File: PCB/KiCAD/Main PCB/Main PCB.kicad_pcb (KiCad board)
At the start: 2 copper layers, 120 x 120 mm, 0 parts

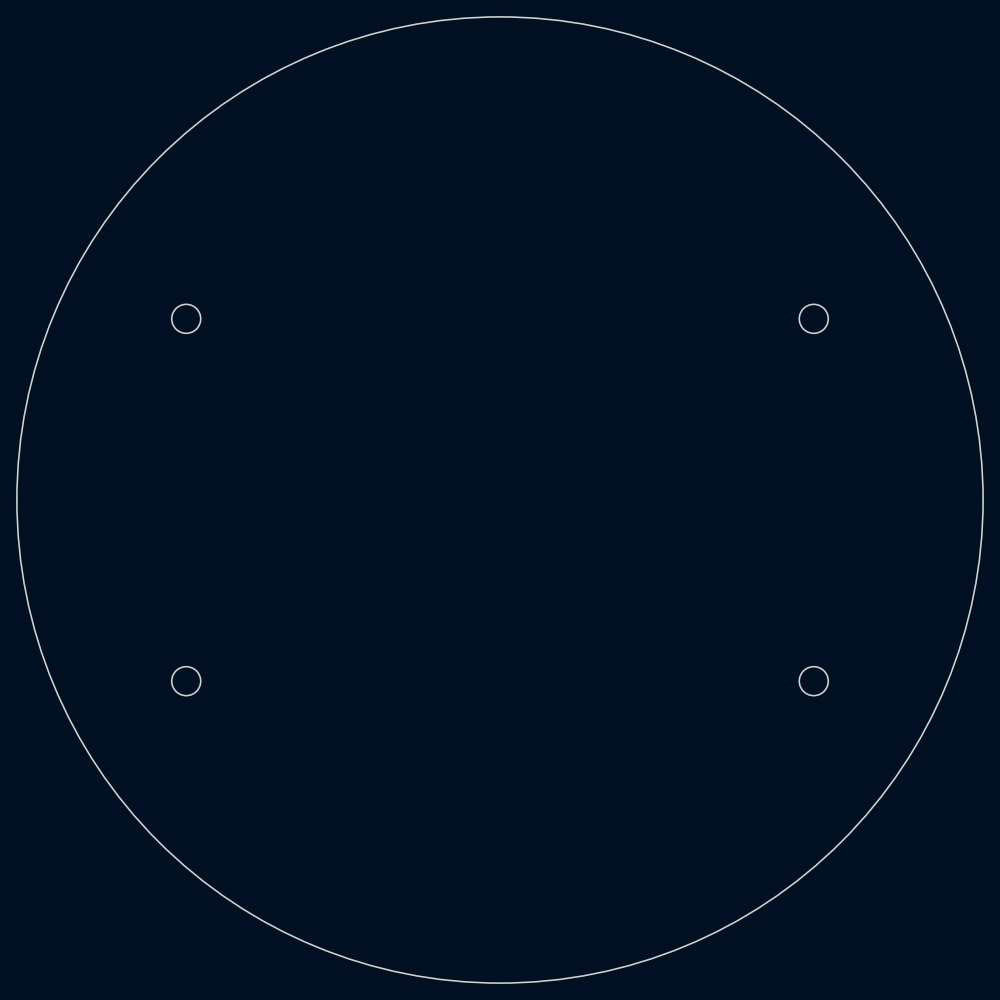
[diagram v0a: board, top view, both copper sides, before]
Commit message: Start to upper PCB
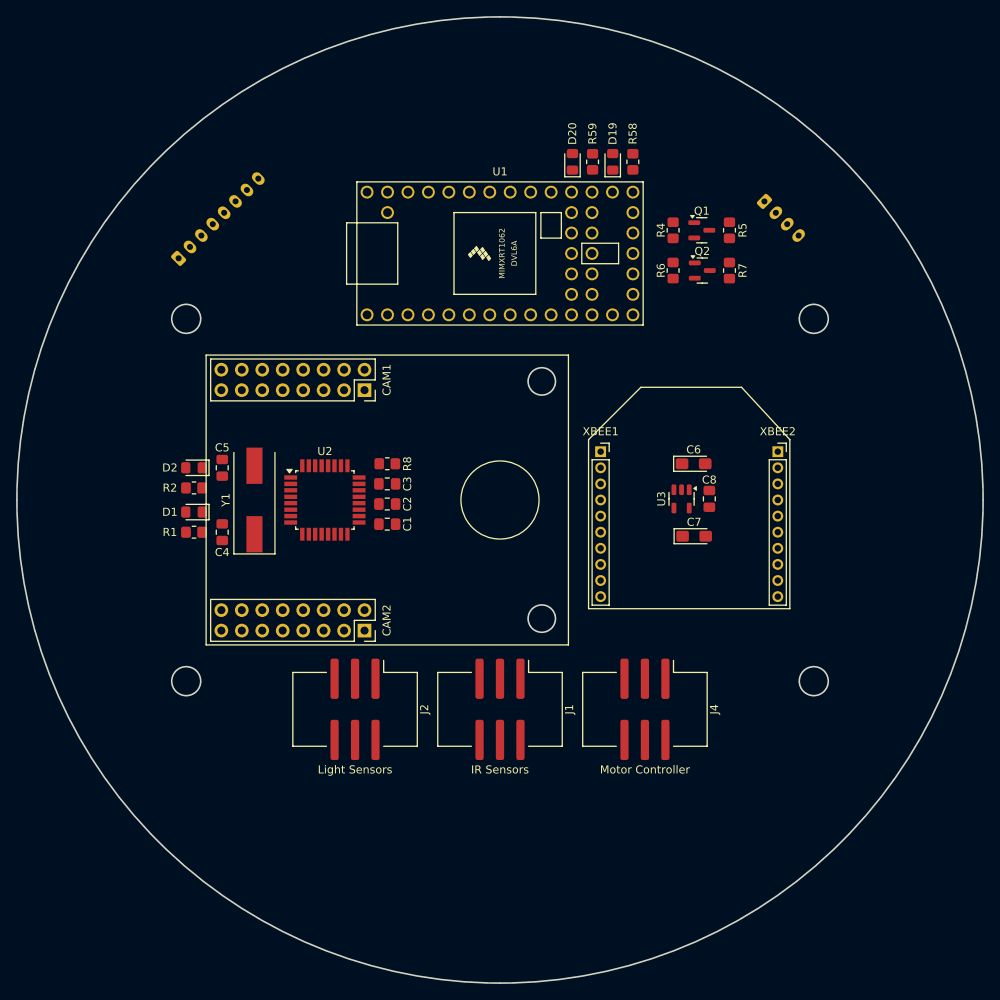
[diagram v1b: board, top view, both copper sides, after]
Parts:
- added C1: 100nF, Capacitor_SMD:C_0805_2012Metric_Pad1.18x1.45mm_HandSolder, F.Cu at (-14.0, 3.00)
- added C2: 100nF, Capacitor_SMD:C_0805_2012Metric_Pad1.18x1.45mm_HandSolder, F.Cu at (-14.0, 0.50)
- added C3: 100nF, Capacitor_SMD:C_0805_2012Metric_Pad1.18x1.45mm_HandSolder, F.Cu at (-14.0, -2.00)
- added C4: 22pF, Capacitor_SMD:C_0805_2012Metric_Pad1.18x1.45mm_HandSolder, F.Cu at (-34.5, 4.00)
- added C5: 22pF, Capacitor_SMD:C_0805_2012Metric_Pad1.18x1.45mm_HandSolder, F.Cu at (-34.5, -4.00)
- added C6: 10uF, Capacitor_Tantalum_SMD:CP_EIA-3216-12_Kemet-S_Pad1.58x1.35mm_HandSolder, F.Cu at (24.1, -4.50)
- added C7: 10uF, Capacitor_Tantalum_SMD:CP_EIA-3216-12_Kemet-S_Pad1.58x1.35mm_HandSolder, F.Cu at (24.1, 4.50)
- added C8: 0.1uF, Capacitor_SMD:C_0805_2012Metric_Pad1.18x1.45mm_HandSolder, F.Cu at (26.0, -0.14)
- added CAM1: Conn_02x08_Top_Bottom, Connector_PinSocket_2.54mm:PinSocket_2x08_P2.54mm_Vertical, F.Cu at (-16.8, -13.6)
- added CAM2: Conn_02x08_Top_Bottom, Connector_PinSocket_2.54mm:PinSocket_2x08_P2.54mm_Vertical, F.Cu at (-16.8, 16.2)
- added D1: GREEN_LED, LED_SMD:LED_0805_2012Metric_Pad1.15x1.40mm_HandSolder, F.Cu at (-38.0, 1.50)
- added D19: RED_LED, LED_SMD:LED_0805_2012Metric_Pad1.15x1.40mm_HandSolder, F.Cu at (14.0, -42.0)
- added D2: RED_LED, LED_SMD:LED_0805_2012Metric_Pad1.15x1.40mm_HandSolder, F.Cu at (-38.0, -4.00)
- added D20: GREEN_LED, LED_SMD:LED_0805_2012Metric_Pad1.15x1.40mm_HandSolder, F.Cu at (9.00, -42.0)
- added J1: Conn_02x03_Odd_Even, Connector_IDC:IDC-Header_2x03_P2.54mm_Vertical_SMD, F.Cu at (0.00, 26.0)
- added J2: Conn_02x03_Odd_Even, Connector_IDC:IDC-Header_2x03_P2.54mm_Vertical_SMD, F.Cu at (-18.0, 26.0)
- added J3: Conn_01x04, Connector_JST:JST_PH_B4B-PH-K_1x04_P2.00mm_Vertical, B.Cu at (32.8, -37.1)
- added J4: Conn_02x03_Odd_Even, Connector_IDC:IDC-Header_2x03_P2.54mm_Vertical_SMD, F.Cu at (18.0, 26.0)
- added J5: Conn_01x08, Connector_JST:JST_PH_B8B-PH-K_1x08_P2.00mm_Vertical, B.Cu at (-39.9, -30.0)
- added Q1: BSS138, Package_TO_SOT_SMD:SOT-23, F.Cu at (25.1, -33.5)
- added Q2: BSS138, Package_TO_SOT_SMD:SOT-23, F.Cu at (25.1, -28.5)
- added R1: 330, Resistor_SMD:R_0805_2012Metric_Pad1.20x1.40mm_HandSolder, F.Cu at (-38.0, 4.00)
- added R2: 330, Resistor_SMD:R_0805_2012Metric_Pad1.20x1.40mm_HandSolder, F.Cu at (-38.0, -1.50)
- added R4: 10k, Resistor_SMD:R_0805_2012Metric_Pad1.20x1.40mm_HandSolder, F.Cu at (21.5, -33.5)
- added R5: 10k, Resistor_SMD:R_0805_2012Metric_Pad1.20x1.40mm_HandSolder, F.Cu at (28.5, -33.5)
- added R58: 330, Resistor_SMD:R_0805_2012Metric_Pad1.20x1.40mm_HandSolder, F.Cu at (16.5, -42.0)
- added R59: 330, Resistor_SMD:R_0805_2012Metric_Pad1.20x1.40mm_HandSolder, F.Cu at (11.5, -42.0)
- added R6: 10k, Resistor_SMD:R_0805_2012Metric_Pad1.20x1.40mm_HandSolder, F.Cu at (21.5, -28.5)
- added R7: 10k, Resistor_SMD:R_0805_2012Metric_Pad1.20x1.40mm_HandSolder, F.Cu at (28.5, -28.5)
- added R8: 10k, Resistor_SMD:R_0805_2012Metric_Pad1.20x1.40mm_HandSolder, F.Cu at (-14.0, -4.50)
- added U1: Teensy4.0, Teensy:Teensy40, F.Cu at (0.00, -30.6)
- added U2: ATmega328PB-A, Package_QFP:TQFP-32_7x7mm_P0.8mm, F.Cu at (-21.8, 0.00)
- added U3: MIC5219-3.3YM5, Package_TO_SOT_SMD:SOT-23-5, F.Cu at (22.6, -0.14)
- added XBEE1: Conn_01x10, Connector_PinSocket_2.00mm:PinSocket_1x10_P2.00mm_Vertical, F.Cu at (12.5, -6.00)
- added XBEE2: Conn_01x10, Connector_PinSocket_2.00mm:PinSocket_1x10_P2.00mm_Vertical, F.Cu at (34.5, -6.00)
- added Y1: Crystal, Crystal:Crystal_SMD_HC49-SD, F.Cu at (-30.5, 0.00)
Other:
- outline, holes or cut-outs redrawn
- board text added: "IR Sensors"
- board text added: "Light Sensors"
- board text added: "MISO"
- board text added: "MOSI"
- board text added: "Motor Controller"
- board text added: "RESET"
- board text added: "SCK"
- board text added: "U1"
- board text added: "U6"

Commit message: More work to main PCB
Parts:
- added C32: 100nF, Capacitor_SMD:C_0805_2012Metric_Pad1.18x1.45mm_HandSolder, F.Cu at (-13.0, 7.50)
- added C33: 100nF, Capacitor_SMD:C_0805_2012Metric_Pad1.18x1.45mm_HandSolder, F.Cu at (-13.0, -7.00)
- added C9: C_Polarized, Capacitor_SMD:CP_Elec_4x5.4, F.Cu at (0.50, 49.5)
- added IC1: TSSP4038, TSOP4038:TSSP4038, F.Cu at (0.54, 56.0)
- added IC2: ADG608BRZ, ADG608BRZ:SOIC127P600X175-16N, F.Cu at (-6.00, 7.50)
- added IC3: ADG608BRZ, ADG608BRZ:SOIC127P600X175-16N, F.Cu at (-6.00, -7.00)
- added R19: 100, Resistor_SMD:R_0805_2012Metric_Pad1.20x1.40mm_HandSolder, F.Cu at (5.50, 53.0)
- moved C1 1.00 mm to (-14.0, 4.00)
- moved C2 1.00 mm to (-14.0, 1.50)
- moved C3 1.00 mm to (-14.0, -1.00)
- moved R8 1.00 mm to (-14.0, -3.50)
- moved U3 0.57 mm to (22.0, 0.00)
- moved C8 0.14 mm to (26.0, 0.00)
- moved C7 0.11 mm to (24.0, 4.50)
- moved C6 0.05 mm to (24.0, -4.50)

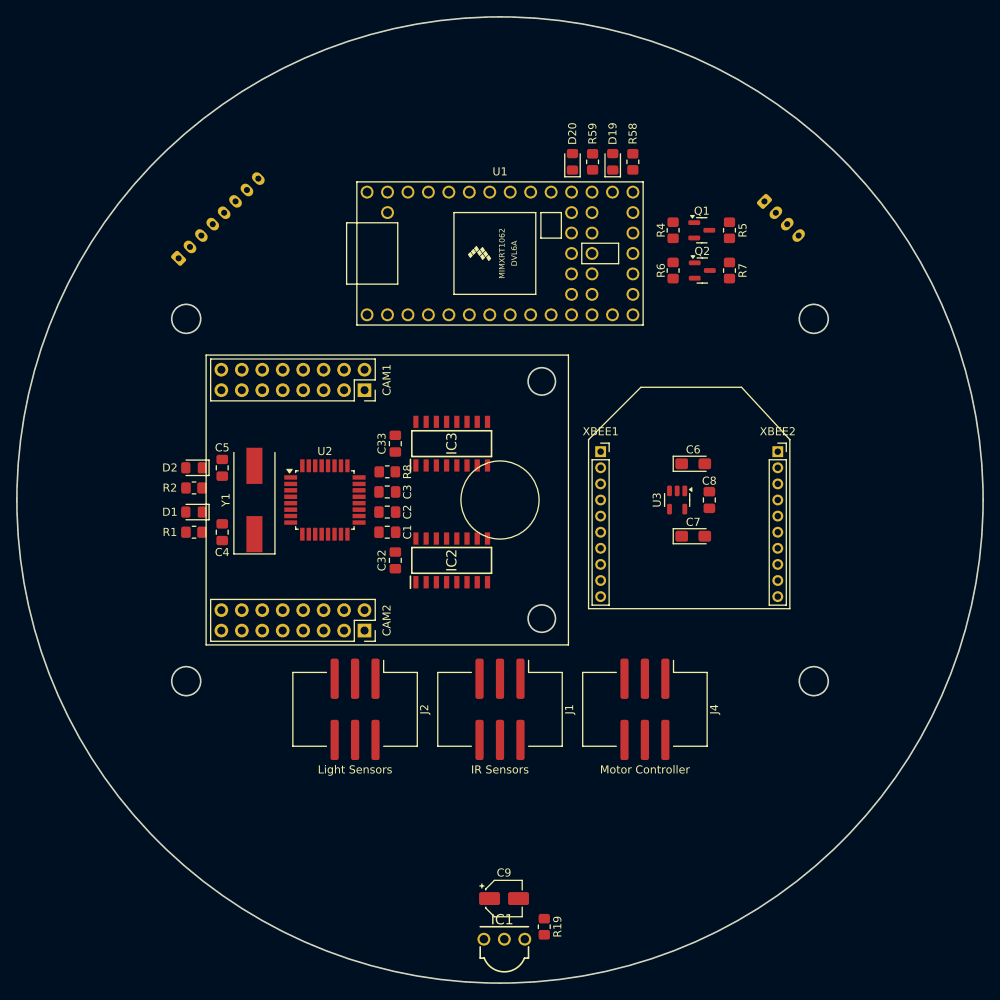
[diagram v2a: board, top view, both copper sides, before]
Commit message: More work to the Main PCB and refinement of Via sizes
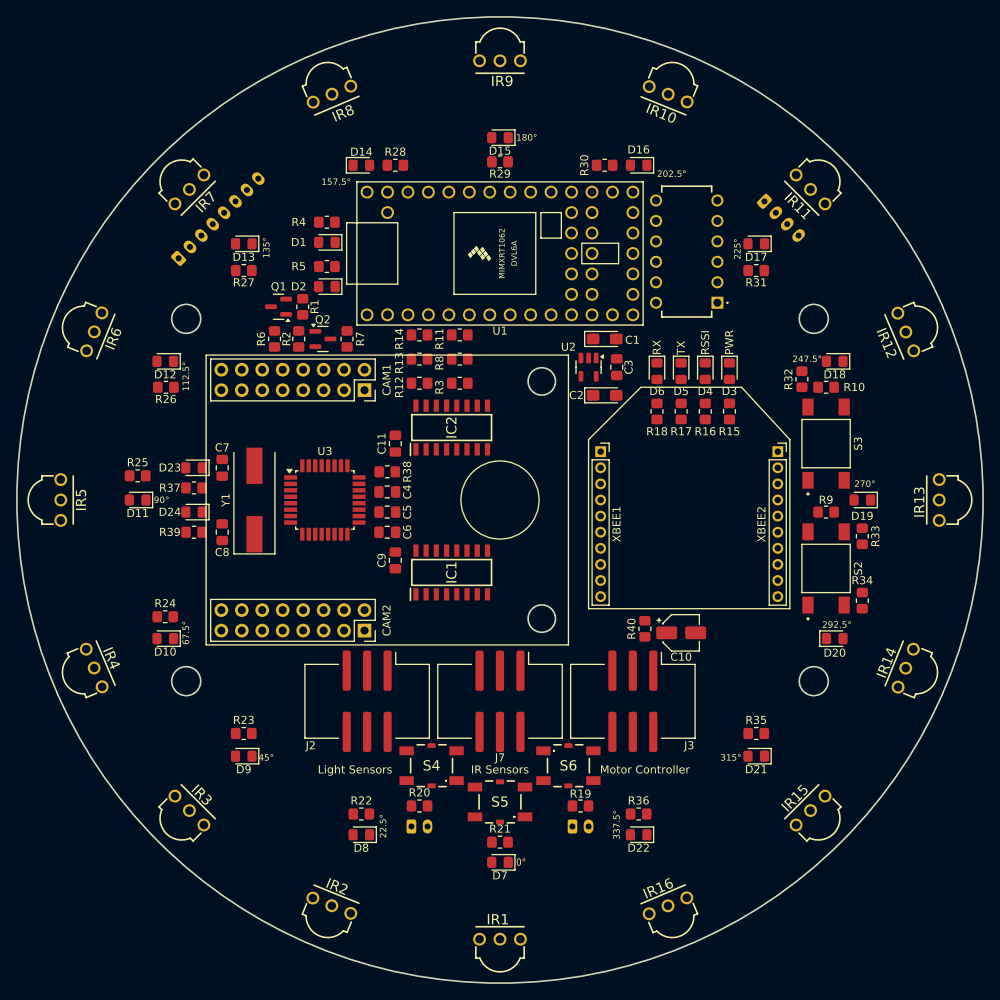
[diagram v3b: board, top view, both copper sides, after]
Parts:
- added D10: BALL_DIR_LED, LED_SMD:LED_0805_2012Metric_Pad1.15x1.40mm_HandSolder, F.Cu at (-41.6, 17.2)
- added D11: BALL_DIR_LED, LED_SMD:LED_0805_2012Metric_Pad1.15x1.40mm_HandSolder, F.Cu at (-45.0, 0.00)
- added D12: BALL_DIR_LED, LED_SMD:LED_0805_2012Metric_Pad1.15x1.40mm_HandSolder, F.Cu at (-41.6, -17.2)
- added D13: BALL_DIR_LED, LED_SMD:LED_0805_2012Metric_Pad1.15x1.40mm_HandSolder, F.Cu at (-31.8, -31.8)
- added D14: BALL_DIR_LED, LED_SMD:LED_0805_2012Metric_Pad1.15x1.40mm_HandSolder, F.Cu at (-17.2, -41.6)
- added D15: BALL_DIR_LED, LED_SMD:LED_0805_2012Metric_Pad1.15x1.40mm_HandSolder, F.Cu at (0.00, -45.0)
- added D16: BALL_DIR_LED, LED_SMD:LED_0805_2012Metric_Pad1.15x1.40mm_HandSolder, F.Cu at (17.2, -41.6)
- added D17: BALL_DIR_LED, LED_SMD:LED_0805_2012Metric_Pad1.15x1.40mm_HandSolder, F.Cu at (31.8, -31.8)
- added D18: BALL_DIR_LED, LED_SMD:LED_0805_2012Metric_Pad1.15x1.40mm_HandSolder, F.Cu at (41.6, -17.2)
- added D19: BALL_DIR_LED, LED_SMD:LED_0805_2012Metric_Pad1.15x1.40mm_HandSolder, F.Cu at (45.0, 0.00)
- added D20: BALL_DIR_LED, LED_SMD:LED_0805_2012Metric_Pad1.15x1.40mm_HandSolder, F.Cu at (41.6, 17.2)
- added D21: BALL_DIR_LED, LED_SMD:LED_0805_2012Metric_Pad1.15x1.40mm_HandSolder, F.Cu at (31.8, 31.8)
- added D22: BALL_DIR_LED, LED_SMD:LED_0805_2012Metric_Pad1.15x1.40mm_HandSolder, F.Cu at (17.2, 41.6)
- added D3: LED, LED_SMD:LED_0805_2012Metric_Pad1.15x1.40mm_HandSolder, F.Cu at (28.5, -16.0)
- added D4: LED, LED_SMD:LED_0805_2012Metric_Pad1.15x1.40mm_HandSolder, F.Cu at (25.5, -16.0)
- added D5: LED, LED_SMD:LED_0805_2012Metric_Pad1.15x1.40mm_HandSolder, F.Cu at (22.5, -16.0)
- added D6: LED, LED_SMD:LED_0805_2012Metric_Pad1.15x1.40mm_HandSolder, F.Cu at (19.5, -16.0)
- added D7: BALL_DIR_LED, LED_SMD:LED_0805_2012Metric_Pad1.15x1.40mm_HandSolder, F.Cu at (0.00, 45.0)
- added D8: BALL_DIR_LED, LED_SMD:LED_0805_2012Metric_Pad1.15x1.40mm_HandSolder, F.Cu at (-17.2, 41.6)
- added D9: BALL_DIR_LED, LED_SMD:LED_0805_2012Metric_Pad1.15x1.40mm_HandSolder, F.Cu at (-31.8, 31.8)
- added IR10: TSSP4038, TSOP4038:TSSP4038, F.Cu at (21.4, -51.7)
- added IR11: TSSP4038, TSOP4038:TSSP4038, F.Cu at (39.6, -39.6)
- added IR12: TSSP4038, TSOP4038:TSSP4038, F.Cu at (51.7, -21.4)
- added IR13: TSSP4038, TSOP4038:TSSP4038, F.Cu at (56.0, 0.00)
- added IR14: TSSP4038, TSOP4038:TSSP4038, F.Cu at (51.7, 21.4)
- added IR15: TSSP4038, TSOP4038:TSSP4038, F.Cu at (39.6, 39.6)
- added IR16: TSSP4038, TSOP4038:TSSP4038, F.Cu at (21.4, 51.7)
- added IR2: TSSP4038, TSOP4038:TSSP4038, F.Cu at (-21.4, 51.7)
- added IR3: TSSP4038, TSOP4038:TSSP4038, F.Cu at (-39.6, 39.6)
- added IR4: TSSP4038, TSOP4038:TSSP4038, F.Cu at (-51.7, 21.4)
- added IR5: TSSP4038, TSOP4038:TSSP4038, F.Cu at (-56.0, 0.00)
- added IR6: TSSP4038, TSOP4038:TSSP4038, F.Cu at (-51.7, -21.4)
- added IR7: TSSP4038, TSOP4038:TSSP4038, F.Cu at (-39.6, -39.6)
- added IR8: TSSP4038, TSOP4038:TSSP4038, F.Cu at (-21.4, -51.7)
- added IR9: TSSP4038, TSOP4038:TSSP4038, F.Cu at (0.00, -56.0)
- added J5: Conn_01x02, Connector_JST:JST_PH_B2B-PH-K_1x02_P2.00mm_Vertical, B.Cu at (-11.0, 40.5)
- added J6: Conn_01x02, Connector_JST:JST_PH_B2B-PH-K_1x02_P2.00mm_Vertical, B.Cu at (9.00, 40.5)
- added R10: 4.7k, Resistor_SMD:R_0805_2012Metric_Pad1.20x1.40mm_HandSolder, F.Cu at (40.5, -14.0)
- added R11: 4.7k, Resistor_SMD:R_0805_2012Metric_Pad1.20x1.40mm_HandSolder, F.Cu at (-5.00, -20.5)
- added R12: 4.7k, Resistor_SMD:R_0805_2012Metric_Pad1.20x1.40mm_HandSolder, F.Cu at (-10.0, -14.5)
- added R13: 4.7k, Resistor_SMD:R_0805_2012Metric_Pad1.20x1.40mm_HandSolder, F.Cu at (-10.0, -17.5)
- added R14: 4.7k, Resistor_SMD:R_0805_2012Metric_Pad1.20x1.40mm_HandSolder, F.Cu at (-10.0, -20.5)
- added R15: 1k, Resistor_SMD:R_0805_2012Metric_Pad1.20x1.40mm_HandSolder, F.Cu at (28.5, -11.0)
- added R16: 1k, Resistor_SMD:R_0805_2012Metric_Pad1.20x1.40mm_HandSolder, F.Cu at (25.5, -11.0)
- added R17: 1k, Resistor_SMD:R_0805_2012Metric_Pad1.20x1.40mm_HandSolder, F.Cu at (22.5, -11.0)
- added R18: 1k, Resistor_SMD:R_0805_2012Metric_Pad1.20x1.40mm_HandSolder, F.Cu at (19.5, -11.0)
- added R19: 10k, Resistor_SMD:R_0805_2012Metric_Pad1.20x1.40mm_HandSolder, F.Cu at (10.0, 38.0)
- added R20: 82, Resistor_SMD:R_0805_2012Metric_Pad1.20x1.40mm_HandSolder, F.Cu at (-10.0, 38.0)
- added R21: 130, Resistor_SMD:R_0805_2012Metric_Pad1.20x1.40mm_HandSolder, F.Cu at (0.00, 42.5)
- added R22: 130, Resistor_SMD:R_0805_2012Metric_Pad1.20x1.40mm_HandSolder, F.Cu at (-17.2, 39.0)
- added R23: 130, Resistor_SMD:R_0805_2012Metric_Pad1.20x1.40mm_HandSolder, F.Cu at (-31.8, 29.0)
- added R24: 130, Resistor_SMD:R_0805_2012Metric_Pad1.20x1.40mm_HandSolder, F.Cu at (-41.6, 14.5)
- added R25: 130, Resistor_SMD:R_0805_2012Metric_Pad1.20x1.40mm_HandSolder, F.Cu at (-45.0, -3.00)
- added R26: 130, Resistor_SMD:R_0805_2012Metric_Pad1.20x1.40mm_HandSolder, F.Cu at (-41.5, -14.0)
- added R27: 130, Resistor_SMD:R_0805_2012Metric_Pad1.20x1.40mm_HandSolder, F.Cu at (-31.8, -28.5)
- added R28: 130, Resistor_SMD:R_0805_2012Metric_Pad1.20x1.40mm_HandSolder, F.Cu at (-13.0, -41.6)
- added R29: 130, Resistor_SMD:R_0805_2012Metric_Pad1.20x1.40mm_HandSolder, F.Cu at (0.00, -42.0)
- added R3: 4.7k, Resistor_SMD:R_0805_2012Metric_Pad1.20x1.40mm_HandSolder, F.Cu at (-5.00, -14.5)
- added R30: 130, Resistor_SMD:R_0805_2012Metric_Pad1.20x1.40mm_HandSolder, F.Cu at (13.0, -41.6)
- added R31: 130, Resistor_SMD:R_0805_2012Metric_Pad1.20x1.40mm_HandSolder, F.Cu at (31.8, -28.5)
- added R32: 130, Resistor_SMD:R_0805_2012Metric_Pad1.20x1.40mm_HandSolder, F.Cu at (37.5, -15.0)
- added R33: 130, Resistor_SMD:R_0805_2012Metric_Pad1.20x1.40mm_HandSolder, F.Cu at (45.0, 4.50)
- added R34: 130, Resistor_SMD:R_0805_2012Metric_Pad1.20x1.40mm_HandSolder, F.Cu at (45.0, 12.5)
- added R35: 130, Resistor_SMD:R_0805_2012Metric_Pad1.20x1.40mm_HandSolder, F.Cu at (31.8, 29.0)
- added R36: 130, Resistor_SMD:R_0805_2012Metric_Pad1.20x1.40mm_HandSolder, F.Cu at (17.2, 39.0)
- added R8: 4.7k, Resistor_SMD:R_0805_2012Metric_Pad1.20x1.40mm_HandSolder, F.Cu at (-5.00, -17.5)
- added R9: 4.7k, Resistor_SMD:R_0805_2012Metric_Pad1.20x1.40mm_HandSolder, F.Cu at (40.5, 1.50)
- added S1: 2454982-4, DIP_SW_6:DIP_6_SWITCH_THT, F.Cu at (27.0, -24.5)
- added S2: TS04-SMT, TS04:SW_TS04-66-70-BK-260-SMT, F.Cu at (40.5, 8.50)
- added S3: TS04-SMT, TS04:SW_TS04-66-70-BK-260-SMT, F.Cu at (40.5, -7.00)
- added S4: MSLPT5252BG4MTR, MSLPT5252BG4MTR:MSLPT5252BG4MTR, F.Cu at (-8.50, 33.0)
- added S5: MSLPT5252BG4MTR, MSLPT5252BG4MTR:MSLPT5252BG4MTR, F.Cu at (0.00, 37.5)
- added S6: MSLPT5252BG4MTR, MSLPT5252BG4MTR:MSLPT5252BG4MTR, F.Cu at (8.50, 33.0)
- C10: renamed from C9; value C_Polarized -> 4.7uF
- moved R6 58.1 mm to (-28.0, -20.0), turned to 90 degrees
- moved Q1 53.4 mm to (-27.5, -24.0), turned to 180 degrees
- moved R7 48.3 mm to (-19.0, -20.0)
- moved Q2 47.9 mm to (-22.0, -20.0)
- moved R2 47.3 mm to (-25.0, -20.0)
- moved R1 47.0 mm to (-24.5, -24.0)
- moved C10 39.7 mm to (22.5, 16.5)
- moved R40 39.1 mm to (18.0, 16.0), turned to 90 degrees
- moved R4 38.7 mm to (-21.5, -34.5), turned to 180 degrees
- moved D1 36.9 mm to (-21.5, -32.0), turned to 180 degrees
- moved R5 35.5 mm to (-21.5, -29.0), turned to 180 degrees
- moved D2 34.2 mm to (-21.5, -26.5), turned to 180 degrees
- moved C2 20.7 mm to (13.0, -13.0)
- moved C3 20.1 mm to (14.5, -16.5)
- moved U2 19.8 mm to (11.0, -16.5)
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- renumbered C6 to C1, C33 to C11, C7 to C2, C8 to C3, C3 to C4, C2 to C5, C1 to C6, C5 to C7, C4 to C8, C32 to C9, D19 to D1, D20 to D2, D2 to D23, D1 to D24, IC2 to IC1, IC3 to IC2, IC1 to IR1, J3 to J1, J4 to J3, J5 to J4, J1 to J7, R4 to R1, R6 to R2, R2 to R37, R8 to R38, R1 to R39, R58 to R4, R19 to R40, R59 to R5, R5 to R6, U3 to U2, U2 to U3
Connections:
- net Net-(IC1-VS) renamed TSSP_PWR
- net Net-(J1-Pin_5) renamed RESET_U2
- IC1 pad 10: unconnected-(IC2-S7-Pad10) -> Net-(IC1-S7)
- IC1 pad 11: unconnected-(IC2-S6-Pad11) -> Net-(IC1-S6)
- IC1 pad 12: unconnected-(IC2-S5-Pad12) -> Net-(IC1-S5)
- IC1 pad 5: unconnected-(IC2-S2-Pad5) -> Net-(IC1-S2)
- IC1 pad 6: unconnected-(IC2-S3-Pad6) -> Net-(IC1-S3)
- IC1 pad 7: unconnected-(IC2-S4-Pad7) -> Net-(IC1-S4)
- IC1 pad 9: unconnected-(IC2-S8-Pad9) -> Net-(IC1-S8)
- IC2 pad 10: unconnected-(IC3-S7-Pad10) -> Net-(IC2-S7)
- IC2 pad 11: unconnected-(IC3-S6-Pad11) -> Net-(IC2-S6)
- IC2 pad 12: unconnected-(IC3-S5-Pad12) -> Net-(IC2-S5)
- IC2 pad 4: unconnected-(IC3-S1-Pad4) -> Net-(IC2-S1)
- IC2 pad 5: unconnected-(IC3-S2-Pad5) -> Net-(IC2-S2)
- IC2 pad 6: unconnected-(IC3-S3-Pad6) -> Net-(IC2-S3)
- IC2 pad 7: unconnected-(IC3-S4-Pad7) -> Net-(IC2-S4)
- IC2 pad 9: unconnected-(IC3-S8-Pad9) -> Net-(IC2-S8)
- U1 pad 10: unconnected-(U1-8_TX2_IN1-Pad10) -> CAMERA_TX
- U1 pad 12: unconnected-(U1-10_CS_MQSR-Pad12) -> START_BUTTON
- U1 pad 13: unconnected-(U1-11_MOSI_CTX1-Pad13) -> CALIBRATE_BUTTON
- U1 pad 14: unconnected-(U1-12_MISO_MQSL-Pad14) -> IR_DIR_0
- U1 pad 2: unconnected-(U1-0_RX1_CRX2_CS1-Pad2) -> COM_RX
- U1 pad 21: unconnected-(U1-14_A0_TX3_SPDIF_OUT-Pad21) -> LG_RECEIVE
- U1 pad 22: unconnected-(U1-15_A1_RX3_SPDIF_IN-Pad22) -> IR_DIR_90
- U1 pad 23: unconnected-(U1-16_A2_RX4_SCL1-Pad23) -> IR_DIR_180
- U1 pad 24: unconnected-(U1-17_A3_TX4_SDA1-Pad24) -> IR_DIR_270
- U1 pad 27: unconnected-(U1-20_A6_TX5_LRCLK1-Pad27) -> IR_DIR_45
- U1 pad 28: unconnected-(U1-21_A7_RX5_BCLK1-Pad28) -> IR_DIR_135
- U1 pad 29: unconnected-(U1-22_A8_CTX1-Pad29) -> IR_DIR_225
- U1 pad 3: unconnected-(U1-1_TX1_CTX2_MISO1-Pad3) -> COM_TX
- U1 pad 30: unconnected-(U1-23_A9_CRX1_MCLK1-Pad30) -> IR_DIR_315
- U1 pad 35: unconnected-(U1-24_A10_TX6_SCL2-Pad35) -> IR_DIR_22.5
- U1 pad 36: unconnected-(U1-25_A11_RX6_SDA2-Pad36) -> IR_DIR_67.5
- U1 pad 37: unconnected-(U1-26_A12_MOSI1-Pad37) -> IR_DIR_112.5
- U1 pad 38: unconnected-(U1-27_A13_SCK1-Pad38) -> IR_DIR_157.5
- U1 pad 39: unconnected-(U1-28_RX7-Pad39) -> IR_DIR_202.5
- U1 pad 4: unconnected-(U1-2_OUT2-Pad4) -> Net-(U1-2_OUT2)
- U1 pad 40: unconnected-(U1-29_TX7-Pad40) -> IR_DIR_247.5
- U1 pad 41: unconnected-(U1-30_CRX3-Pad41) -> IR_DIR_292.5
- U1 pad 42: unconnected-(U1-31_CTX3-Pad42) -> IR_DIR_337.5
- U1 pad 43: unconnected-(U1-32_OUT1B-Pad43) -> Net-(U1-32_OUT1B)
- U1 pad 5: unconnected-(U1-3_LRCLK2-Pad5) -> Net-(U1-3_LRCLK2)
- U1 pad 6: unconnected-(U1-4_BCLK2-Pad6) -> Net-(U1-4_BCLK2)
- U1 pad 7: unconnected-(U1-5_IN2-Pad7) -> Net-(U1-5_IN2)
- U1 pad 8: unconnected-(U1-6_OUT1D-Pad8) -> Net-(U1-6_OUT1D)
- U1 pad 9: unconnected-(U1-7_RX2_OUT1A-Pad9) -> CAMERA_RX
- XBEE1 pad 1: +3V3 -> +3V3_XBEE
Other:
- board text added: "0°"
- board text added: "112.5°"
- board text added: "135°"
- board text added: "157.5°"
- board text added: "180°"
- board text added: "202.5°"
- board text added: "22.5°"
- board text added: "225°"
- board text added: "247.5°"
- board text added: "270°"
- board text added: "292.5°"
- board text added: "315°"
- board text added: "337.5°"
- board text added: "45°"
- board text added: "67.5°"
- board text added: "90°"
- board text added: "PWR"
- board text added: "RSSI"
- board text added: "RX"
- board text added: "TX"
